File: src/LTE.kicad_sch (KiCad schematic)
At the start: 32 parts, among them J8 Conn_Coaxial, J9 SIM_NANO_Socket, Q7 BC817-40-7-F, Q8 BC817-40-7-F, Q9 BC817-40-7-F, U15 TXS0104ERGYR

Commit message: ongoing work
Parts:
- removed J8: Conn_Coaxial, 7Sigma:SMA-SMD_BWSMA-KE-P001, symbol Connectors:BWSMA-KE-P001
- removed Q9: BC817-40-7-F, 7Sigma:SOT-23-3, symbol Transistors:BC817-40-7-F
- removed R48: 10K, 7Sigma:R_0402_1005Metric, symbol Resistor:0402WGF1002TCE
- added J4: Conn_Coaxial, 7Sigma:SMA-SMD_BWSMA-KE-P001, symbol Connectors:BWSMA-KE-P001
- added Q18: SI2308A, 7Sigma:SOT-23-3, symbol Transistors:SI2308A
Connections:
- net LED_STAT: now also R47.1, Q18.1 (G)
- net RF_ANT: now also J4.1 (In)
- net at R20.2: now also Q18.3 (D)
- net +3V3 renamed 3V3
- net 3V3: no longer C44.1, C45.1
- net GNDD renamed GND
- net GND: now also J4.2 (Ext), Q18.2 (S)
- new net 3V8: C44.1, C45.1
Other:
- removed sheet EG915U
- removed sheet LE310X1
- added sheet LE910R1 (LE910R1.kicad_sch)
- moved on the sheet: C44, C45, D3, J9, R20, R45, R47, TP13, TP14, TP15, TP16, TP17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

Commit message: Layout progress
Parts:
- C44, C45: Price @1 USD (none) -> 0.6789; Price @100 USD (none) -> 0.4372; Price @Bulk USD (none) -> 0.3827; Price Bulk Qty (none) -> 1000; Price Source (none) -> LCSC; Price Updated (none) -> 2026-05-14
- C50, C51: Price @1 USD (none) -> 0.0015; Price @100 USD (none) -> 0.0015; Price @Bulk USD (none) -> 0.0012; Price Bulk Qty (none) -> 1000; Price Source (none) -> LCSC; Price Updated (none) -> 2026-05-14
- C52, C53: Price @1 USD (none) -> 0.0016; Price @100 USD (none) -> 0.0016; Price @Bulk USD (none) -> 0.0013; Price Bulk Qty (none) -> 1000; Price Source (none) -> LCSC; Price Updated (none) -> 2026-05-14
- D3: Price @1 USD (none) -> 0.0396; Price @100 USD (none) -> 0.0396; Price @Bulk USD (none) -> 0.0266; Price Bulk Qty (none) -> 600; Price Source (none) -> LCSC; Price Updated (none) -> 2026-05-14
- J4: Price @1 USD (none) -> 0.3843; Price @100 USD (none) -> 0.2076; Price @Bulk USD (none) -> 0.1897; Price Bulk Qty (none) -> 1000; Price Source (none) -> LCSC; Price Updated (none) -> 2026-05-14
- J9: Price @1 USD (none) -> 0.1994; Price @100 USD (none) -> 0.1579; Price @Bulk USD (none) -> 0.1180; Price Bulk Qty (none) -> 500; Price Source (none) -> LCSC; Price Updated (none) -> 2026-05-14
- Q18: Price @1 USD (none) -> 0.0364; Price @100 USD (none) -> 0.0284; Price @Bulk USD (none) -> 0.0242; Price Bulk Qty (none) -> 300; Price Source (none) -> LCSC; Price Updated (none) -> 2026-05-14
- Q7, Q8: Price @1 USD (none) -> 0.1029; Price @100 USD (none) -> 0.0828; Price @Bulk USD (none) -> 0.0653; Price Bulk Qty (none) -> 500; Price Source (none) -> LCSC; Price Updated (none) -> 2026-05-14
- R20: Price @1 USD (none) -> 0.0011; Price @100 USD (none) -> 0.0011; Price @Bulk USD (none) -> 0.0009; Price Bulk Qty (none) -> 1000; Price Source (none) -> LCSC; Price Updated (none) -> 2026-05-14
- R33, R34, R47: Price @1 USD (none) -> 0.0009; Price @100 USD (none) -> 0.0009; Price @Bulk USD (none) -> 0.0007; Price Bulk Qty (none) -> 1000; Price Source (none) -> LCSC; Price Updated (none) -> 2026-05-14
- R35, R36, R45: Price @1 USD (none) -> 0.0013; Price @100 USD (none) -> 0.0013; Price @Bulk USD (none) -> 0.0011; Price Bulk Qty (none) -> 1000; Price Source (none) -> LCSC; Price Updated (none) -> 2026-05-14
- U15: footprint 7Sigma:VQFN-14_L3.5-W3.5-P0.50-BL-EP -> 7Sigma:VQFN-14_L3.5-W3.5-P0.50-BL-EP-ThermalVias; Price @1 USD (none) -> 0.3795; Price @100 USD (none) -> 0.2997; Price @Bulk USD (none) -> 0.1940; Price Bulk Qty (none) -> 500; Price Source (none) -> LCSC; Price Updated (none) -> 2026-05-14
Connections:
- net PWR_MON: no longer TP13.1, U15.2 (A1)
- new net LTE_PWR_MON: TP13.1, U15.2 (A1)

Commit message: floorplan changed, check in
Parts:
- removed C44, C45: 470uF, 7Sigma:CP_Elec_10x10, symbol Capacitor:EEHZK1E471P
- added C44, C45, C55, C56, C57: 47uF, 7Sigma:C_1210_3225Metric, symbol Capacitor:CS3225X7R476K160NRL
- J9: symbol Connectors:NANO SIM TL6P H1.35 -> Connectors:NANO_SIM_TL6P_H1.35
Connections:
- net 3V8: now also C44.1, C45.1, C55.1, C56.1, C57.1
- net GND: now also C44.2, C45.2, C55.2, C56.2, C57.2

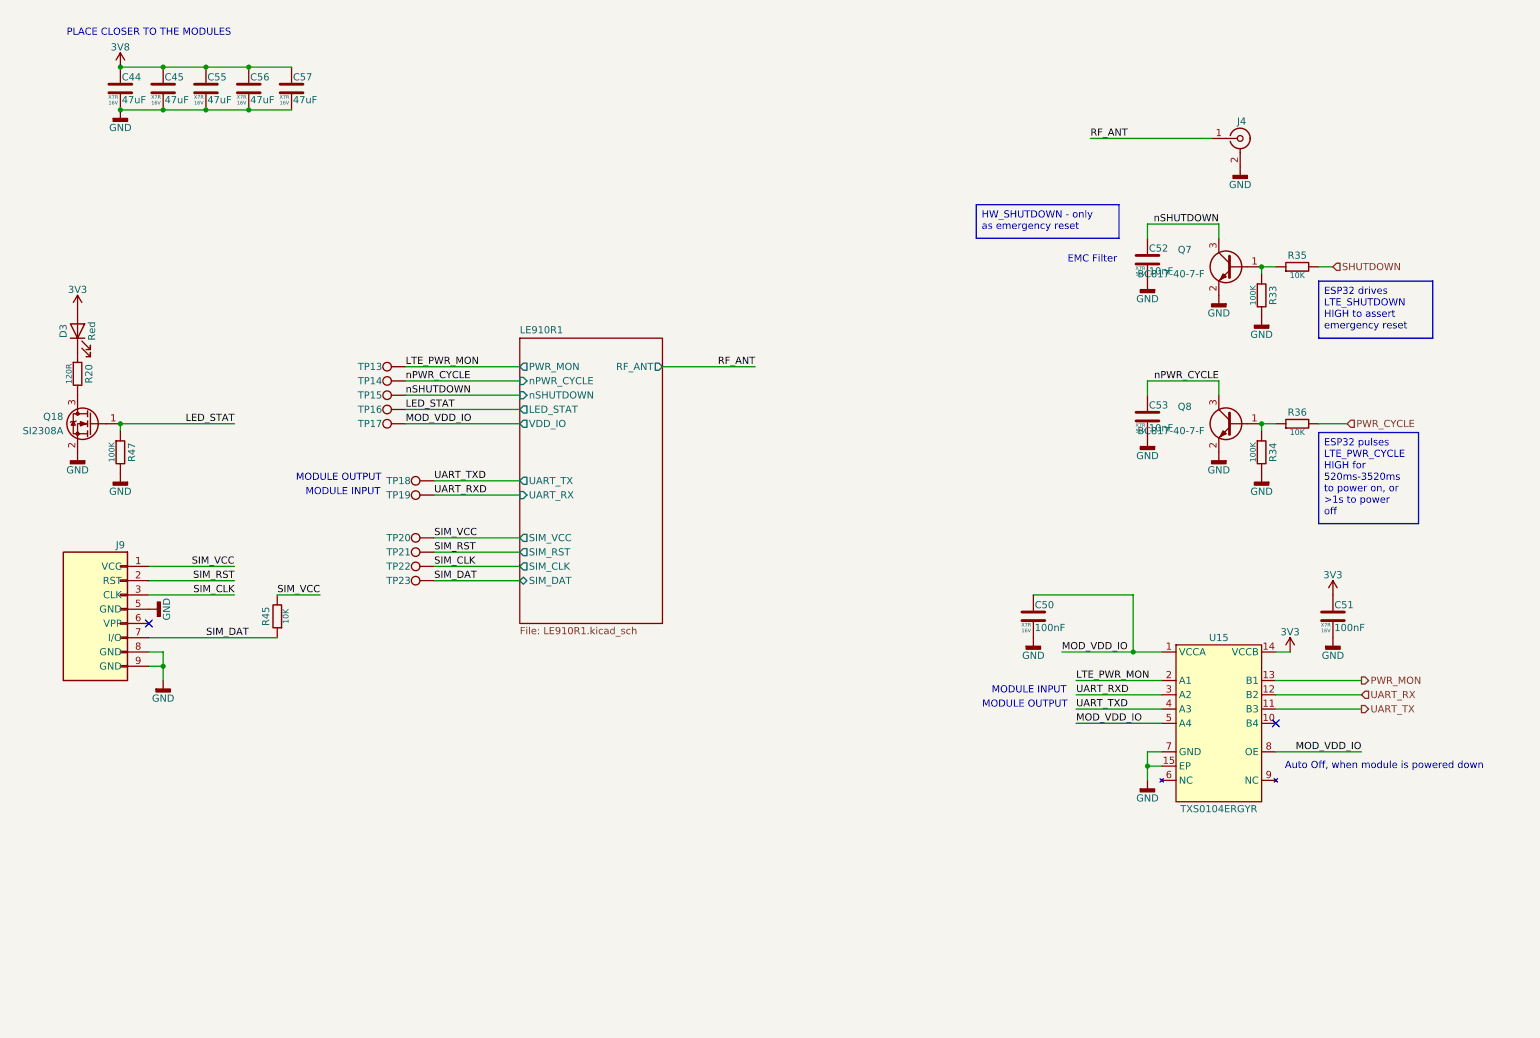
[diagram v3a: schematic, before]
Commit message: schematic cleanup, verification. GPIO9 pin pulldown changed to pullup.
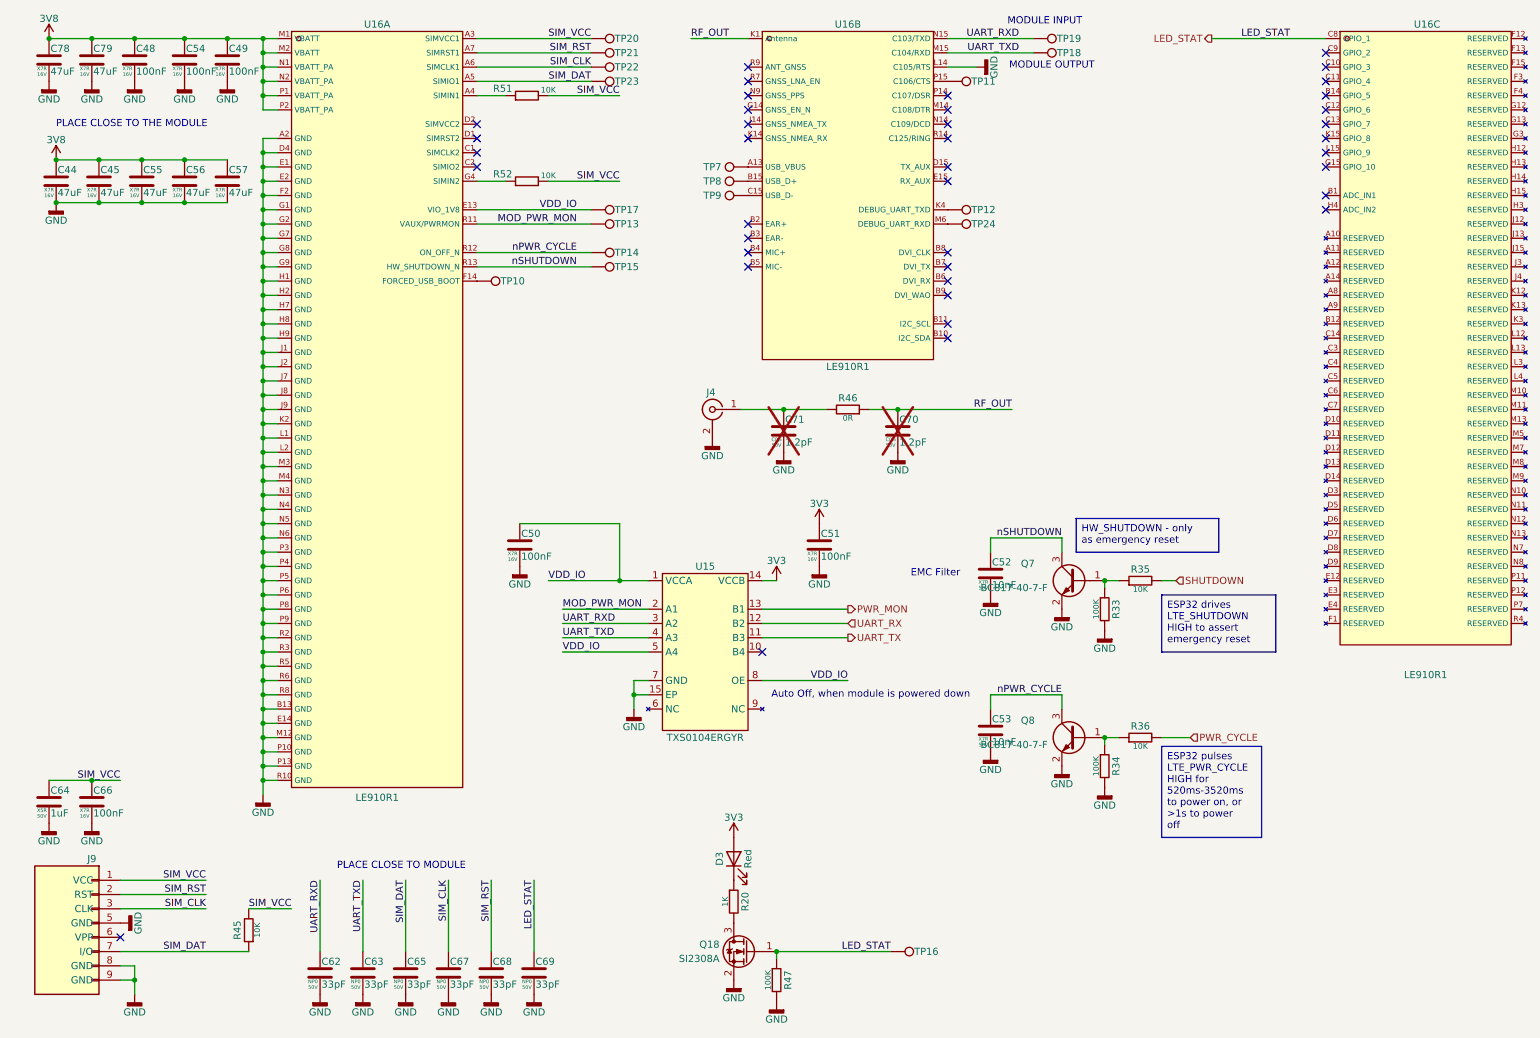
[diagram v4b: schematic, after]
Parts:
- added C48, C49, C54, C66: 100nF, 7Sigma:C_0402_1005Metric, symbol Capacitor:CL05B104KO5NNNC
- added C62, C63, C65, C67, C68, C69: 33pF, 7Sigma:C_0402_1005Metric, symbol Capacitor:CC0402JRNPO9BN330
- added C64: 1uF, 7Sigma:C_0402_1005Metric, symbol Capacitor:GRM155R61H105KE05D
- added C70, C71: 1.2pF, 7Sigma:C_0402_1005Metric, symbol Capacitor:GJM1555C1H1R2WB01D
- added C78, C79: 47uF, 7Sigma:C_1210_3225Metric, symbol Capacitor:CS3225X7R476K160NRL
- added R46: 0R, 7Sigma:R_0402_1005Metric, symbol Resistor:0402WGF0000TCE
- added R51, R52: 10K, 7Sigma:R_0402_1005Metric, symbol Resistor:0402WGF1002TCE
- added TP10, TP11, TP12, TP24, TP7, TP8, TP9: TestPoint, 7Sigma:TestPoint_Pad_D1.5mm, symbol TestPoints:TestPoint_Pad_D1.5mm
- added U16: LE910R1, 7Sigma:XCVR_LE910R1-EU, symbol ICs:LE910R1-EU
- R20: value 120R -> 1K; symbol Resistor:0402WGF1200TCE -> Resistor:0402WGF1001TCE; LCSC Part C25079 -> C11702; Manufacturer Part Number 1 0402WGF1200TCE -> 0402WGF1001TCE; Supplier Part Number 1 C25079 -> C11702
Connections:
- net 3V8: now also C48.1, C49.1, C54.1, C78.1, C79.1, U16.M1 (VBATT), U16.M2 (VBATT), U16.N1 (VBATT_PA), U16.N2 (VBATT_PA), U16.P1 (VBATT_PA), U16.P2 (VBATT_PA)
- net GND: now also C48.2, C49.2, C54.2, C62.2, C63.2, C64.2, C65.2, C66.2, C67.2, C68.2, C69.2, C70.2, C71.2, C78.2, C79.2, U16.A2 (GND), U16.B13 (GND), U16.D4 (GND), U16.E1 (GND), U16.E14 (GND), U16.E2 (GND), U16.F2 (GND), U16.G1 (GND), U16.G2 (GND), U16.G7 (GND), U16.G8 (GND), U16.G9 (GND), U16.H1 (GND), U16.H2 (GND), U16.H7 (GND), U16.H8 (GND), U16.H9 (GND), U16.J1 (GND), U16.J2 (GND), U16.J7 (GND), U16.J8 (GND), U16.J9 (GND), U16.K2 (GND), U16.L1 (GND), U16.L14 (C105/RTS), U16.L2 (GND), U16.M12 (GND), U16.M3 (GND), U16.M4 (GND), U16.N3 (GND), U16.N4 (GND), U16.N5 (GND), U16.N6 (GND), U16.P10 (GND), U16.P13 (GND), U16.P3 (GND), U16.P4 (GND), U16.P5 (GND), U16.P6 (GND), U16.P8 (GND), U16.P9 (GND), U16.R10 (GND), U16.R2 (GND), U16.R3 (GND), U16.R5 (GND), U16.R6 (GND), U16.R8 (GND)
- net LED_STAT: now also C69.1, U16.C8 (GPIO_1)
- net SIM_CLK: now also C67.1, U16.A6 (SIMCLK1)
- net SIM_DAT: now also C65.1, U16.A5 (SIMIO1)
- net SIM_RST: now also C68.1, U16.A7 (SIMRST1)
- net SIM_VCC: now also C64.1, C66.1, R51.2, R52.2, U16.A3 (SIMVCC1)
- net UART_RXD: now also C62.1, U16.N15 (C103/TXD)
- net UART_TXD: now also C63.1, U16.M15 (C104/RXD)
- net nPWR_CYCLE: now also U16.R12 (ON_OFF_N)
- net nSHUTDOWN: now also U16.R13 (HW_SHUTDOWN_N)
- net LTE_PWR_MON renamed MOD_PWR_MON
- net MOD_PWR_MON: now also U16.R11 (VAUX/PWRMON)
- net MOD_VDD_IO renamed VDD_IO
- net VDD_IO: now also U16.E13 (VIO_1V8)
- net RF_ANT: no longer names the net of J4.1 (In)
- net RF_ANT: now also C71.1, R46.2
- new net: TP9.1, U16.C15 (USB_D-)
- new net: TP7.1, U16.A13 (USB_VBUS)
- new net: TP8.1, U16.B15 (USB_D+)
- new net: TP12.1, U16.K4 (DEBUG_UART_TXD)
- new net: TP24.1, U16.M6 (DEBUG_UART_RXD)
- new net: TP11.1, U16.P15 (C106/CTS)
- new net: R52.1, U16.G4 (SIMIN2)
- new net: R51.1, U16.A4 (SIMIN1)
- new net: TP10.1, U16.F14 (FORCED_USB_BOOT)
- new net RF_OUT: C70.1, R46.1, U16.K1 (Antenna)
- no-connect marks 2 -> 39
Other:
- removed sheet LE910R1
- note added: "PLACE CLOSE TO MODULE"
- note added: "PLACE CLOSE TO THE MODULE"
- note removed: "PLACE CLOSER TO THE MODULES"
- moved on the sheet: C44, C45, C50, C51, C52, C53, C55, C56, C57, D3, J4, J9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
